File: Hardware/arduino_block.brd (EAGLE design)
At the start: 30.5 x 62.2 mm, 40 parts, among them U1 MIC5205-3.3V (150mA), U2 EDISON_CONNECTOR_FULLMOUNTING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, U3 EDISON_CONNECTOR_FULLHEADER, U4 ATMEGA328, Y1 8MHZ

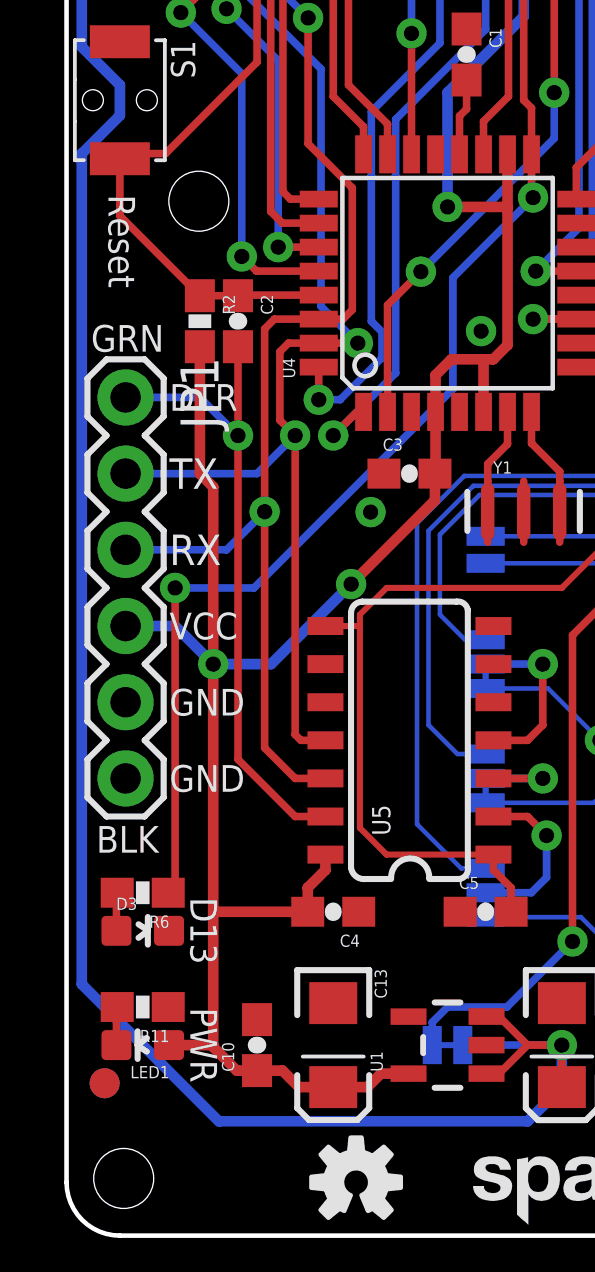
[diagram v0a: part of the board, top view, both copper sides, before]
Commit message: Ready for reds. Moved some silk to be more readable along left edge of board. No known to-do items
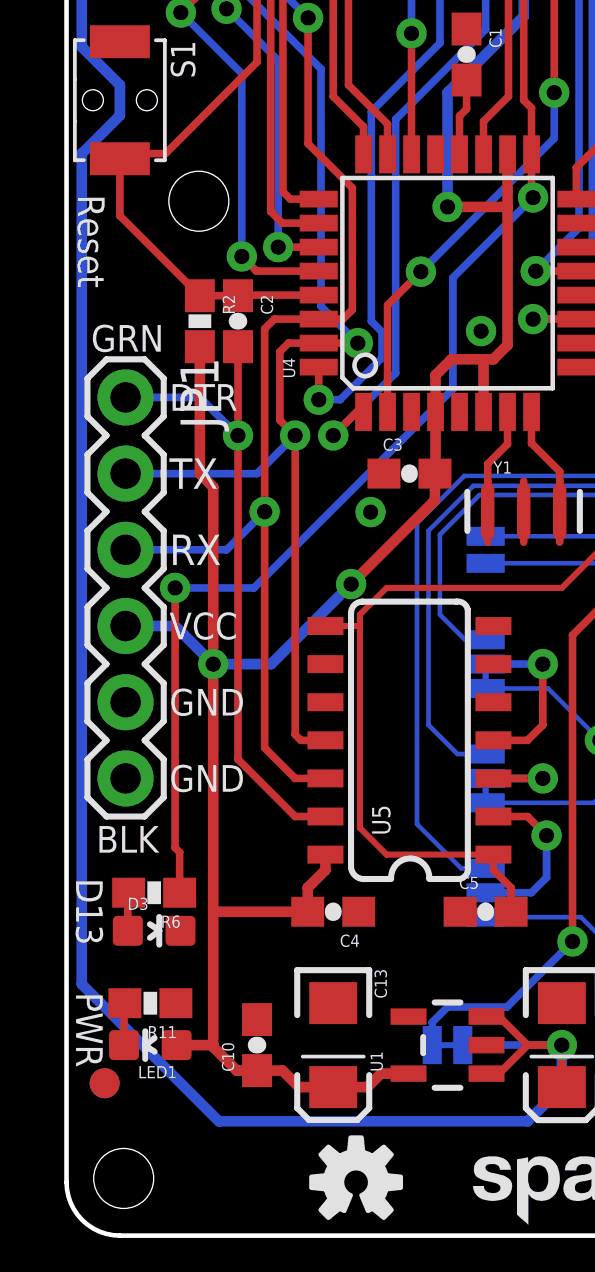
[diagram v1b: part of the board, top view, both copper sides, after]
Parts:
- moved D3 0.38 mm to (2.92, 10.2)
- moved R6 0.38 mm to (2.92, 11.4)
- moved R11 0.28 mm to (2.79, 7.75)
- moved LED1 0.25 mm to (2.79, 6.35)
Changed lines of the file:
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@@
 <?xml version="1.0" encoding="utf-8"?>
 <!DOCTYPE eagle SYSTEM "eagle.dtd">
-<eagle version="7.1.0">
+<eagle version="6.6.0">
 <drawing>
 <settings>
@@
 <setting verticaltext="up"/>
 </settings>
-<grid distance="0.05" unitdist="inch" unit="inch" style="lines" multiple="1" display="yes" altdistance="0.0025" altunitdist="inch" altunit="inch"/>
+<grid distance="0.05" unitdist="inch" unit="inch" style="lines" multiple="1" display="yes" altdistance="0.005" altunitdist="inch" altunit="inch"/>
 <layers>
-<layer number="1" name="Top" color="4" fill="1" visible="yes" active="yes"/>
+<layer number="1" name="Top" color="4" fill="1" visible="no" active="yes"/>
 <layer number="2" name="Route2" color="1" fill="3" visible="no" active="yes"/>
 <layer number="15" name="Route15" color="4" fill="6" visible="no" active="yes"/>
@@
 <layer number="19" name="Unrouted" color="6" fill="1" visible="yes" active="yes"/>
 <layer number="20" name="Dimension" color="15" fill="1" visible="yes" active="yes"/>
-<layer number="21" name="tPlace" color="16" fill="1" visible="yes" active="yes"/>
+<layer number="21" name="tPlace" color="16" fill="1" visible="no" active="yes"/>
 <layer number="22" name="bPlace" color="14" fill="1" visible="yes" active="yes"/>
-<layer number="23" name="tOrigins" color="15" fill="1" visible="yes" active="yes"/>
+<layer number="23" name="tOrigins" color="15" fill="1" visible="no" active="yes"/>
 <layer number="24" name="bOrigins" color="15" fill="1" visible="yes" active="yes"/>
 <layer number="25" name="tNames" color="7" fill="1" visible="no" active="yes"/>
@@
 <layer number="43" name="vRestrict" color="2" fill="10" visible="no" active="yes"/>
 <layer number="44" name="Drills" color="7" fill="1" visible="no" active="yes"/>
-<layer number="45" name="Holes" color="7" fill="1" visible="yes" active="yes"/>
+<layer number="45" name="Holes" color="7" fill="1" visible="no" active="yes"/>
 <layer number="46" name="Milling" color="3" fill="1" visible="no" active="yes"/>
-<layer number="51" name="tDocu" color="6" fill="1" visible="yes" active="yes"/>
+<layer number="51" name="tDocu" color="6" fill="1" visible="no" active="yes"/>
 <layer number="3" name="Route3" color="4" fill="3" visible="no" active="no"/>
 <layer number="4" name="Route4" color="1" fill="4" visible="no" active="no"/>
@@
 <text x="3.429" y="20.32" size="0.889" layer="21" font="vector" ratio="15" align="center-left">VCC</text>
 <text x="3.429" y="17.78" size="0.889" layer="21" font="vector" ratio="15" align="center-left">GND</text>
-<text x="2.286" y="33.147" size="0.889" layer="21" font="vector" ratio="15" rot="SR270" align="top-center">Reset</text>
+<text x="1.27" y="33.147" size="0.889" layer="21" font="vector" ratio="15" rot="SR270" align="top-center">Reset</text>
 <text x="2.032" y="13.6525" size="0.889" layer="21" font="vector" ratio="15" align="top-center">BLK</text>
 <text x="11.43" y="6.35" size="0.8128" layer="22" font="vector" ratio="15" rot="MR0" align="center-left">VSYS</text>
-<text x="4.572" y="6.35" size="0.889" layer="21" font="vector" ratio="15" rot="SR270" align="center">PWR</text>
-<text x="4.572" y="10.16" size="0.889" layer="21" font="vector" ratio="15" rot="SR270" align="center">D13</text>
+<text x="0.762" y="6.858" size="0.889" layer="21" font="vector" ratio="15" rot="SR270" align="center">PWR</text>
+<text x="0.762" y="10.795" size="0.889" layer="21" font="vector" ratio="15" rot="SR270" align="center">D13</text>
 <text x="12.7" y="18.161" size="0.8128" layer="22" font="vector" ratio="15" rot="MR0" align="center-left">UART1</text>
 <text x="12.7" y="19.939" size="0.8128" layer="22" font="vector" ratio="15" rot="MR0" align="center-left">UART2</text>
@@
 <pass name="Default">
 <param name="RoutingGrid" value="50mil"/>
-<param name="AutoGrid" value="1"/>
-<param name="Efforts" value="0"/>
-<param name="TopRouterVariant" value="1"/>
 <param name="tpViaShape" value="round"/>
 <param name="PrefDir.1" value="|"/>
@@
 <element name="C10" library="SparkFun" package="0603-CAP" value="0.1uF" x="6.35" y="6.35" rot="R90"/>
 <element name="C13" library="SparkFun" package="EIA3216" value="10uF" x="8.89" y="6.35" rot="R270"/>
-<element name="R11" library="SparkFun" package="0603-RES" value="10K" x="2.54" y="7.62" rot="R180"/>
-<element name="LED1" library="Testing" package="0603-LED-ALT1" value="Red" x="2.54" y="6.35" rot="R90"/>
+<element name="R11" library="SparkFun" package="0603-RES" value="10K" x="2.794" y="7.747" rot="R180"/>
+<element name="LED1" library="Testing" package="0603-LED-ALT1" value="Red" x="2.794" y="6.35" rot="R90"/>
 <element name="R2" library="SparkFun" package="0603-RES" value="10K" x="4.445" y="30.48" rot="R270"/>
 <element name="C3" library="SparkFun" package="0603-CAP" value="0.1uF" x="11.43" y="25.4"/>
 <element name="C1" library="SparkFun" package="0603-CAP" value="0.1uF" x="13.335" y="39.37" rot="R270"/>
-<element name="R6" library="SparkFun" package="0603-RES" value="330" x="2.54" y="11.43" rot="R180"/>
-<element name="D3" library="Testing" package="0603-LED-ALT1" value="Green" x="2.54" y="10.16" rot="R270"/>
+<element name="R6" library="SparkFun" package="0603-RES" value="330" x="2.921" y="11.43" rot="R180"/>
+<element name="D3" library="Testing" package="0603-LED-ALT1" value="Green" x="2.921" y="10.16" rot="R270"/>
 <element name="U1" library="SparkFun" package="SOT23-5" value="MIC5205-3.3V (150mA)" x="12.7" y="6.35" rot="R90"/>
 <element name="C19" library="SparkFun" package="EIA3216" value="10uF" x="16.51" y="6.35" rot="R270"/>
@@
 <wire x1="15.5" y1="36.0426" x2="15.5" y2="34.6516" width="0.254" layer="1"/>
 <wire x1="15.5" y1="34.6516" x2="15.5508" y2="34.6008" width="0.254" layer="1"/>
-<wire x1="3.6195" y1="21.59" x2="3.6195" y2="11.6595" width="0.254" layer="1"/>
-<wire x1="3.6195" y1="11.6595" x2="3.39" y2="11.43" width="0.254" layer="1"/>
+<wire x1="3.6195" y1="21.59" x2="3.6195" y2="12.9295" width="0.254" layer="1"/>
 <wire x1="3.6195" y1="21.59" x2="6.2484" y2="21.59" width="0.254" layer="16"/>
 <wire x1="15.5" y1="37.586" x2="15.24" y2="37.846" width="0.254" layer="1"/>
@@
 <wire x1="11.43" y1="48.387" x2="12.446" y2="47.371" width="0.254" layer="1"/>
 <wire x1="12.446" y1="47.371" x2="14.224" y2="47.371" width="0.254" layer="1"/>
+<wire x1="3.771" y1="11.43" x2="3.771" y2="12.778" width="0.254" layer="1"/>
+<wire x1="3.771" y1="12.778" x2="3.6195" y2="12.9295" width="0.254" layer="1"/>
 </signal>
 <signal name="MISO">
@@
 <contactref element="R6" pad="2"/>
 <contactref element="D3" pad="A"/>
-<wire x1="1.663" y1="10.16" x2="1.663" y2="11.403" width="0.254" layer="1"/>
-<wire x1="1.663" y1="11.403" x2="1.69" y2="11.43" width="0.254" layer="1"/>
+<wire x1="2.044" y1="10.16" x2="2.044" y2="11.403" width="0.254" layer="1"/>
+<wire x1="2.044" y1="11.403" x2="2.071" y2="11.43" width="0.254" layer="1"/>
 </signal>
 <signal name="VCC">
@@
 <wire x1="4.445" y1="29.63" x2="4.445" y2="25.4" width="0.3556" layer="1"/>
 <via x="9.486" y="21.717" extent="1-16" drill="0.508"/>
-<wire x1="3.417" y1="6.35" x2="4.8895" y2="6.35" width="0.3556" layer="1"/>
+<wire x1="3.671" y1="6.35" x2="4.8895" y2="6.35" width="0.3556" layer="1"/>
 <wire x1="8.63" y1="12.7" x2="8.63" y2="12.186" width="0.3556" layer="1"/>
 <wire x1="8.63" y1="12.186" x2="8.04" y2="11.596" width="0.3556" layer="1"/>
@@
 <contactref element="R11" pad="2"/>
 <contactref element="LED1" pad="C"/>
-<wire x1="1.663" y1="6.35" x2="1.663" y2="7.593" width="0.254" layer="1"/>
-<wire x1="1.663" y1="7.593" x2="1.69" y2="7.62" width="0.254" layer="1"/>
+<wire x1="1.917" y1="6.35" x2="1.917" y2="7.72" width="0.254" layer="1"/>
+<wire x1="1.917" y1="7.72" x2="1.944" y2="7.747" width="0.254" layer="1"/>
 </signal>
 <signal name="ARD_RX">

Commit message: moved fid
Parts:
- moved FID1 0.51 mm to (1.27, 4.57)
- moved FID3 0.51 mm to (1.27, 4.57)
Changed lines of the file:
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@@
 <setting verticaltext="up"/>
 </settings>
-<grid distance="0.05" unitdist="inch" unit="inch" style="lines" multiple="1" display="yes" altdistance="0.005" altunitdist="inch" altunit="inch"/>
+<grid distance="0.01" unitdist="inch" unit="inch" style="lines" multiple="1" display="yes" altdistance="0.001" altunitdist="inch" altunit="inch"/>
 <layers>
-<layer number="1" name="Top" color="4" fill="1" visible="no" active="yes"/>
-<layer number="2" name="Route2" color="1" fill="3" visible="no" active="yes"/>
-<layer number="15" name="Route15" color="4" fill="6" visible="no" active="yes"/>
+<layer number="1" name="Top" color="4" fill="1" visible="yes" active="yes"/>
+<layer number="2" name="Route2" color="1" fill="3" visible="yes" active="yes"/>
+<layer number="15" name="Route15" color="4" fill="6" visible="yes" active="yes"/>
 <layer number="16" name="Bottom" color="1" fill="1" visible="yes" active="yes"/>
 <layer number="17" name="Pads" color="2" fill="1" visible="yes" active="yes"/>
 <layer number="18" name="Vias" color="2" fill="1" visible="yes" active="yes"/>
 <layer number="19" name="Unrouted" color="6" fill="1" visible="yes" active="yes"/>
-<layer number="20" name="Dimension" color="15" fill="1" visible="yes" active="yes"/>
-<layer number="21" name="tPlace" color="16" fill="1" visible="no" active="yes"/>
-<layer number="22" name="bPlace" color="14" fill="1" visible="yes" active="yes"/>
-<layer number="23" name="tOrigins" color="15" fill="1" visible="no" active="yes"/>
+<layer number="20" name="Dimension" color="6" fill="1" visible="yes" active="yes"/>
+<layer number="21" name="tPlace" color="6" fill="1" visible="yes" active="yes"/>
+<layer number="22" name="bPlace" color="6" fill="1" visible="yes" active="yes"/>
+<layer number="23" name="tOrigins" color="15" fill="1" visible="yes" active="yes"/>
 <layer number="24" name="bOrigins" color="15" fill="1" visible="yes" active="yes"/>
-<layer number="25" name="tNames" color="7" fill="1" visible="no" active="yes"/>
-<layer number="26" name="bNames" color="7" fill="1" visible="no" active="yes"/>
-<layer number="27" name="tValues" color="7" fill="1" visible="no" active="yes"/>
-<layer number="28" name="bValues" color="7" fill="1" visible="no" active="yes"/>
-<layer number="29" name="tStop" color="7" fill="3" visible="no" active="yes"/>
-<layer number="30" name="bStop" color="7" fill="6" visible="no" active="yes"/>
-<layer number="31" name="tCream" color="7" fill="4" visible="no" active="yes"/>
-<layer number="32" name="bCream" color="7" fill="5" visible="no" active="yes"/>
-<layer number="39" name="tKeepout" color="4" fill="11" visible="no" active="yes"/>
-<layer number="40" name="bKeepout" color="1" fill="11" visible="no" active="yes"/>
-<layer number="41" name="tRestrict" color="4" fill="10" visible="no" active="yes"/>
-<layer number="42" name="bRestrict" color="1" fill="10" visible="no" active="yes"/>
-<layer number="43" name="vRestrict" color="2" fill="10" visible="no" active="yes"/>
-<layer number="44" name="Drills" color="7" fill="1" visible="no" active="yes"/>
-<layer number="45" name="Holes" color="7" fill="1" visible="no" active="yes"/>
-<layer number="46" name="Milling" color="3" fill="1" visible="no" active="yes"/>
-<layer number="51" name="tDocu" color="6" fill="1" visible="no" active="yes"/>
+<layer number="25" name="tNames" color="7" fill="1" visible="yes" active="yes"/>
+<layer number="26" name="bNames" color="7" fill="1" visible="yes" active="yes"/>
+<layer number="27" name="tValues" color="7" fill="1" visible="yes" active="yes"/>
+<layer number="28" name="bValues" color="7" fill="1" visible="yes" active="yes"/>
+<layer number="29" name="tStop" color="7" fill="3" visible="yes" active="yes"/>
+<layer number="30" name="bStop" color="7" fill="6" visible="yes" active="yes"/>
+<layer number="31" name="tCream" color="7" fill="4" visible="yes" active="yes"/>
+<layer number="32" name="bCream" color="7" fill="5" visible="yes" active="yes"/>
+<layer number="39" name="tKeepout" color="4" fill="11" visible="yes" active="yes"/>
+<layer number="40" name="bKeepout" color="1" fill="11" visible="yes" active="yes"/>
+<layer number="41" name="tRestrict" color="4" fill="10" visible="yes" active="yes"/>
+<layer number="42" name="bRestrict" color="1" fill="10" visible="yes" active="yes"/>
+<layer number="43" name="vRestrict" color="2" fill="10" visible="yes" active="yes"/>
+<layer number="44" name="Drills" color="7" fill="1" visible="yes" active="yes"/>
+<layer number="45" name="Holes" color="7" fill="1" visible="yes" active="yes"/>
+<layer number="46" name="Milling" color="3" fill="1" visible="yes" active="yes"/>
+<layer number="51" name="tDocu" color="6" fill="1" visible="yes" active="yes"/>
 <layer number="3" name="Route3" color="4" fill="3" visible="no" active="no"/>
 <layer number="4" name="Route4" color="1" fill="4" visible="no" active="no"/>
@@
 <element name="LOGO1" library="SparkFun-Aesthetics" package="OSHW-LOGO-S" value="OSHW-LOGOS" x="9.652" y="1.778"/>
 <element name="LOGO4" library="SparkFun-Aesthetics" package="SFE_LOGO_NAME_FLAME_.1" value="SFE_LOGO_NAME_FLAME.1_INCH" x="13.1064" y="0.254"/>
-<element name="FID1" library="SparkFun-Aesthetics" package="FIDUCIAL-1X2" value="FIDUCIAL1X2" x="1.27" y="5.08"/>
+<element name="FID1" library="SparkFun-Aesthetics" package="FIDUCIAL-1X2" value="FIDUCIAL1X2" x="1.27" y="4.572"/>
 <element name="FID2" library="SparkFun-Aesthetics" package="FIDUCIAL-1X2" value="FIDUCIAL1X2" x="26.67" y="41.91"/>
-<element name="FID3" library="SparkFun-Aesthetics" package="FIDUCIAL-1X2" value="FIDUCIAL1X2" x="1.27" y="5.08" rot="MR0"/>
+<element name="FID3" library="SparkFun-Aesthetics" package="FIDUCIAL-1X2" value="FIDUCIAL1X2" x="1.27" y="4.572" rot="MR0"/>
 <element name="FID4" library="SparkFun-Aesthetics" package="FIDUCIAL-1X2" value="FIDUCIAL1X2" x="26.67" y="41.91" rot="MR0"/>
 <element name="C10" library="SparkFun" package="0603-CAP" value="0.1uF" x="6.35" y="6.35" rot="R90"/>
